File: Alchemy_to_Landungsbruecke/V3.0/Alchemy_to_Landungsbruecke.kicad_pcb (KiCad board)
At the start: 2 copper layers, 38 x 61 mm, 2 parts, among them J1 Conn_02x20_Odd_Even, J2 Conn_02x22_Odd_Even

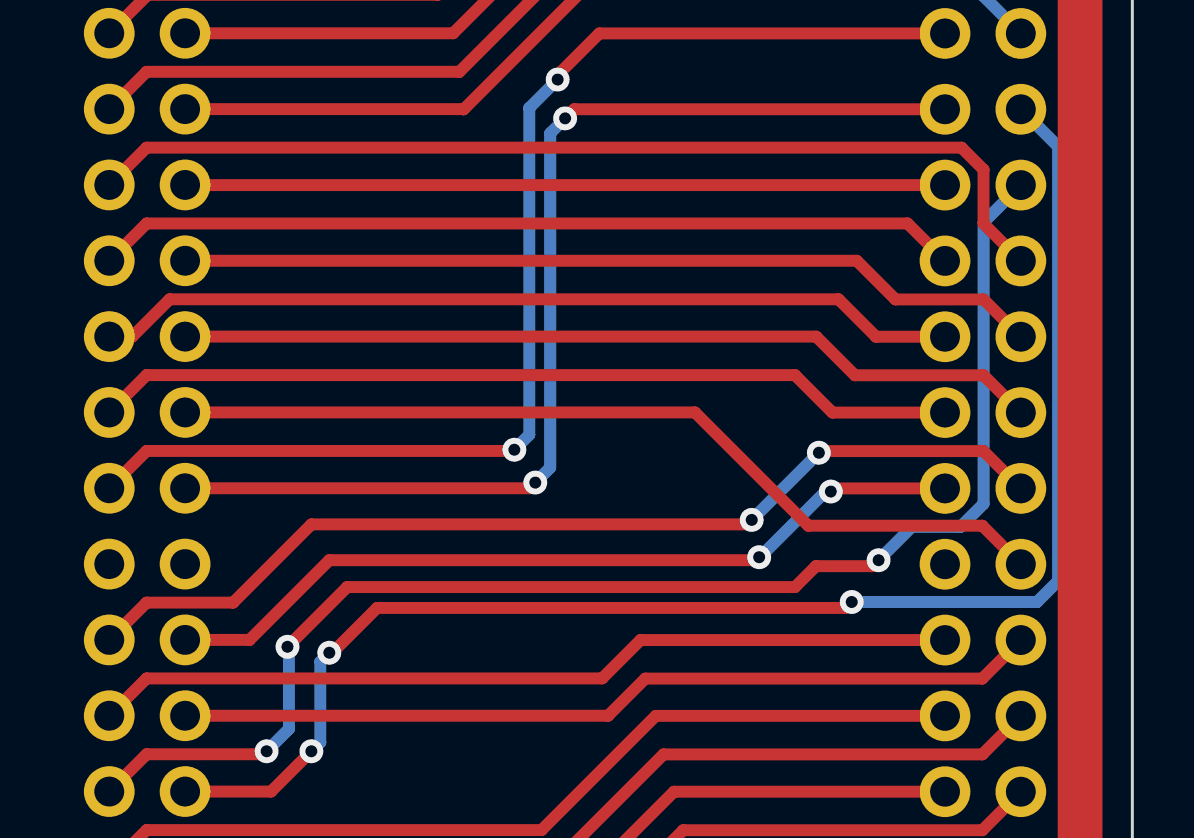
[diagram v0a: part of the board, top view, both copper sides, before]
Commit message: Added 0 ohm resistor to GND for LB CLK
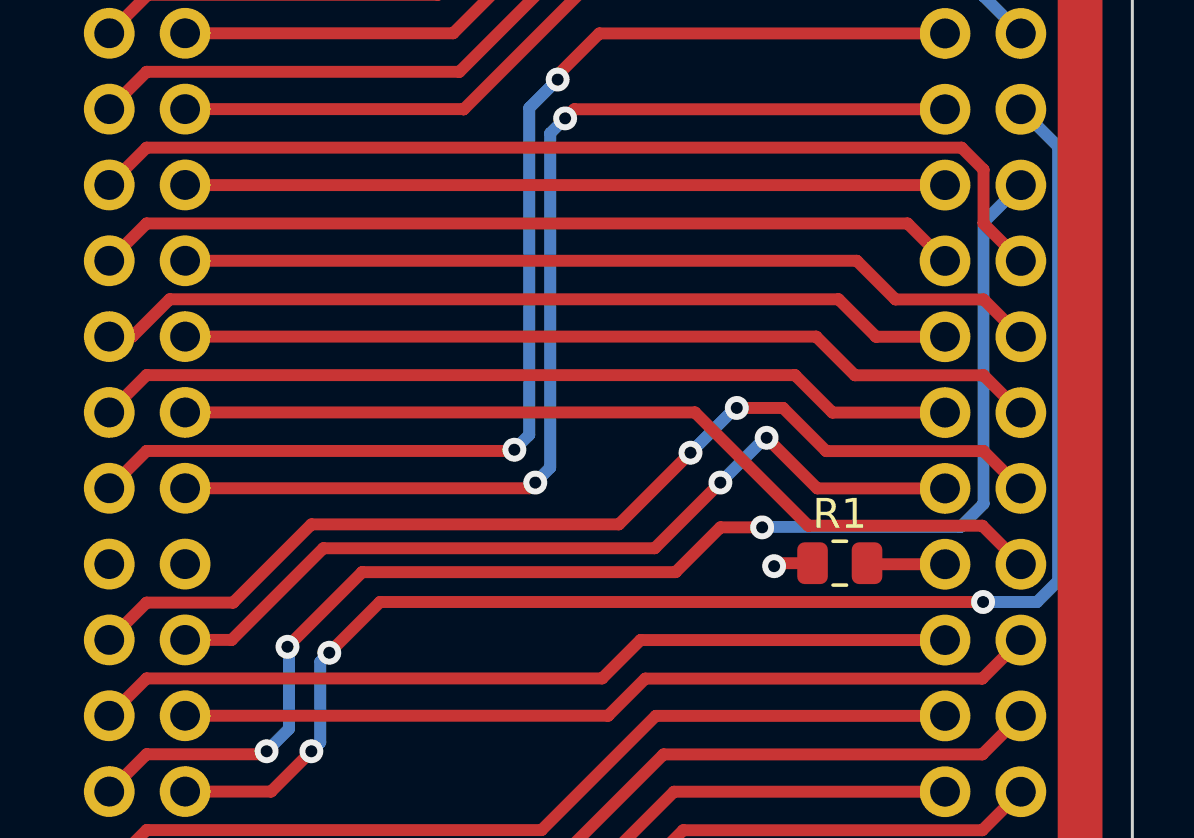
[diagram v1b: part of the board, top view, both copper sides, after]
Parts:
- added R1: 0, Resistor_SMD:R_0805_2012Metric, F.Cu at (160.2, 98.2)
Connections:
- J2 pad 23: unconnected-(J2-Pad23) -> Net-(J2-Pad23)
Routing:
- net Net-(J2-Pad23): track 0.00 -> 2.63 mm
- net /ADC1: track 27.6 -> 29.0 mm
- net GND: track 0.00 -> 1.33 mm, vias 0 -> 1
- net /ADC0: track 33.7 -> 34.9 mm

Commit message: Minor layout fixes
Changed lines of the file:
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@@
       (psa4output false)
       (plotreference true)
-      (plotvalue true)
+      (plotvalue false)
       (plotinvisibletext false)
       (sketchpadsonfab false)
@@
     (fp_line (start -1 0.625) (end -1 -0.625) (layer "F.Fab") (width 0.1))
     (fp_line (start 1 0.625) (end -1 0.625) (layer "F.Fab") (width 0.1))
-    (pad "1" smd roundrect (at -0.9125 0) (size 1.025 1.4) (layers "F.Cu" "F.Paste" "F.Mask") (roundrect_rratio 0.243902)
+    (pad "1" smd roundrect (at -0.9125 0) (size 1.025 1.4) (layers "F.Cu" "F.Paste" "F.Mask") (roundrect_rratio 0.243902439)
       (net 26 "GND") (pintype "passive"))
-    (pad "2" smd roundrect (at 0.9125 0) (size 1.025 1.4) (layers "F.Cu" "F.Paste" "F.Mask") (roundrect_rratio 0.243902)
+    (pad "2" smd roundrect (at 0.9125 0) (size 1.025 1.4) (layers "F.Cu" "F.Paste" "F.Mask") (roundrect_rratio 0.243902439)
       (net 25 "Net-(J2-Pad23)") (pintype "passive"))
     (model "${KICAD6_3DMODEL_DIR}/Resistor_SMD.3dshapes/R_0805_2012Metric.wrl"
